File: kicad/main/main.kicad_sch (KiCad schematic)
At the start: 20 parts, among them U1 DS1813-5+, U2 L7805, U3 Z80CPU, U4 74HC00, U5 AS6C4008-55PCN, U6 74HC273, U7 27C512, X1 4 MHz

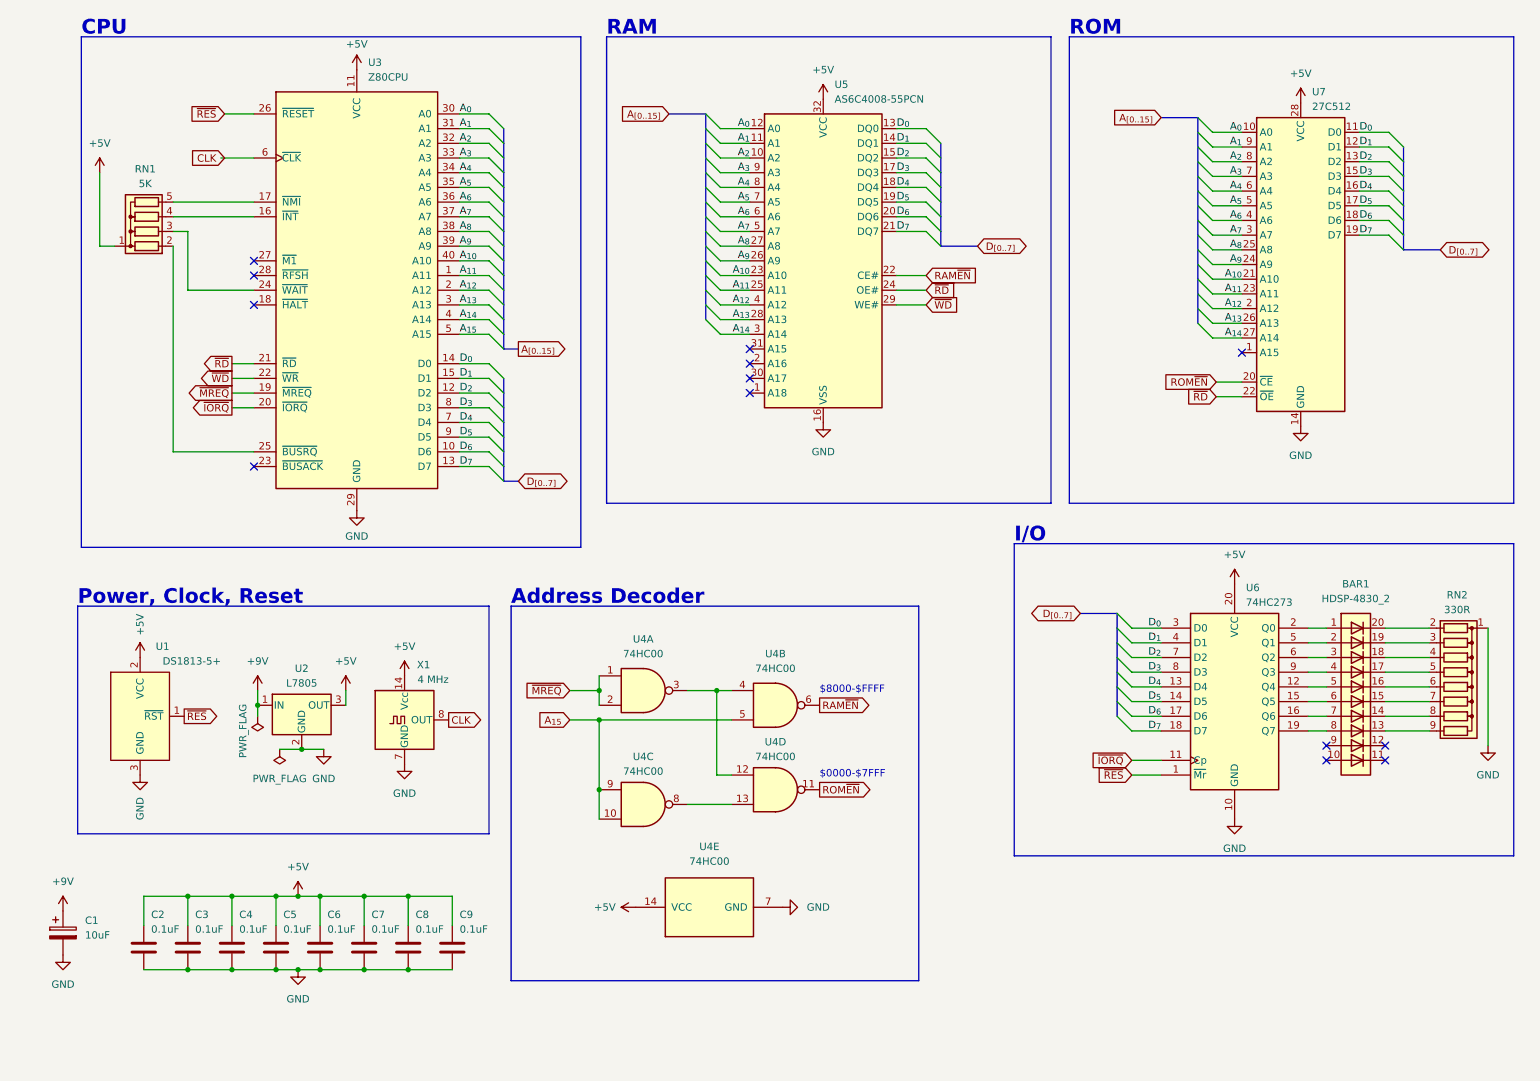
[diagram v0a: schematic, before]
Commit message: Smaller KiCad symbols, reset button
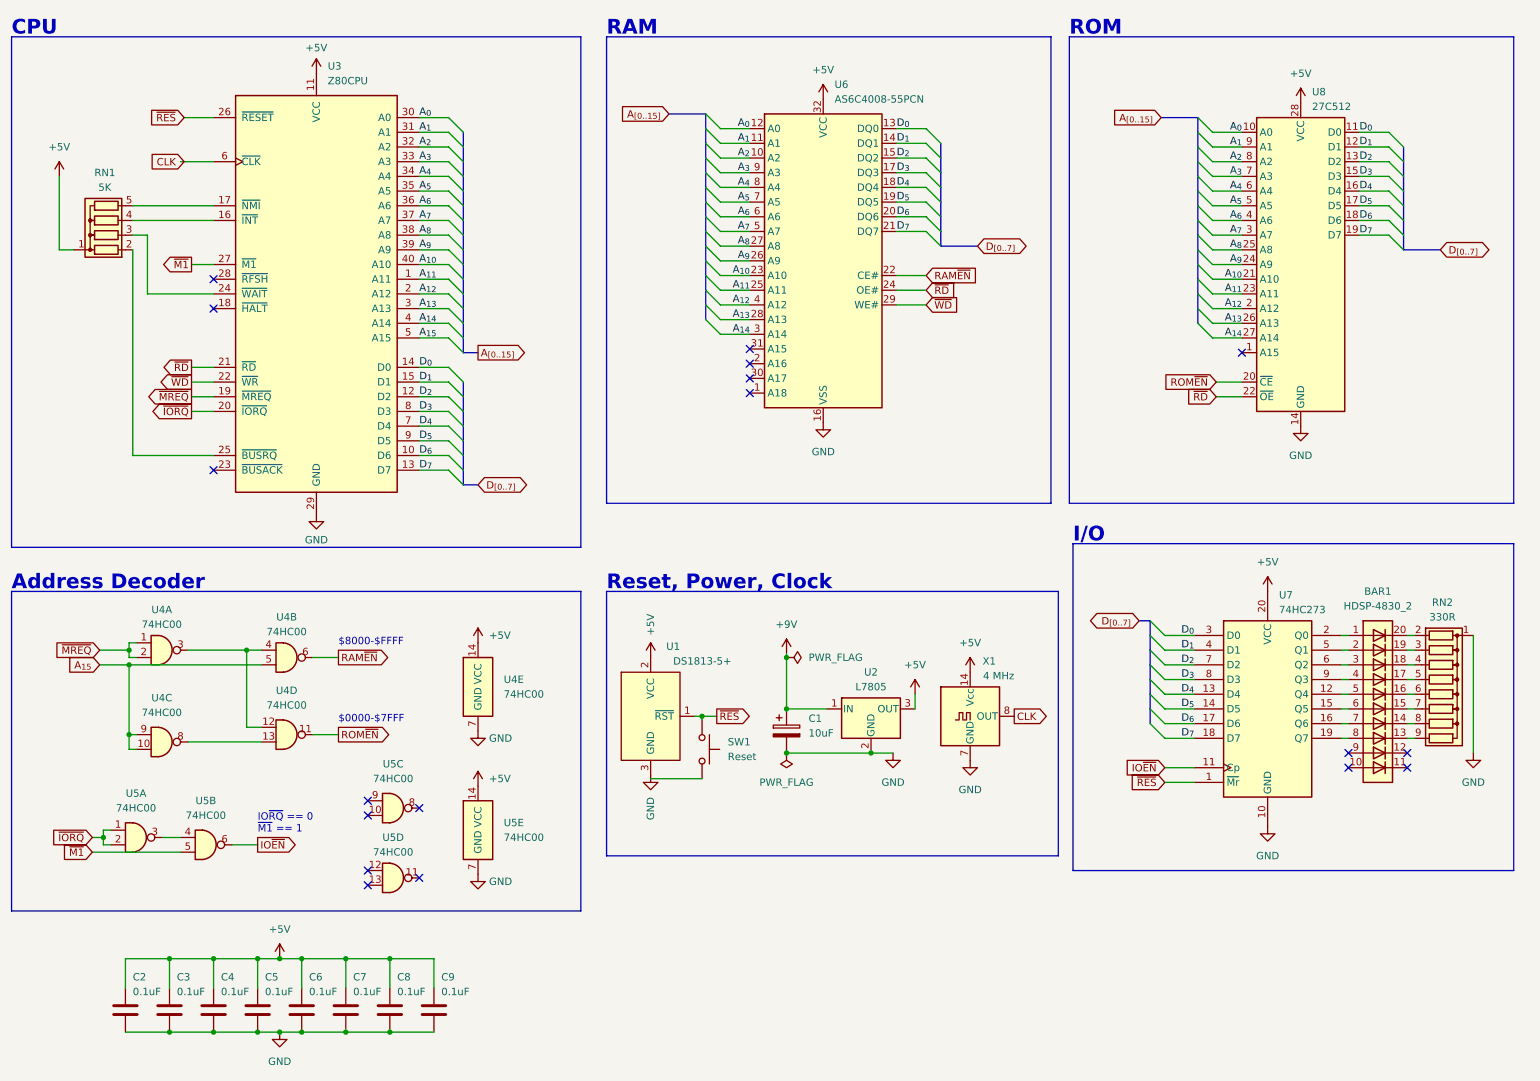
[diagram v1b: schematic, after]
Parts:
- added SW1: Reset, Button_Switch_THT:SW_PUSH_6mm, symbol Switch:SW_Push
- added U5: 74HC00, Package_DIP:DIP-14_W7.62mm_Socket, symbol 74hc00_small:74HC00
- U4: symbol 74xx:74HC00 -> 74hc00_small:74HC00
- renumbered U5 to U6, U6 to U7, U7 to U8
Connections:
- net +5V: now also U5.14 (VCC)
- net GND: now also U5.7 (GND)
- net ~{IORQ}: now also U5.1, U5.2; no longer U7.11 (Cp)
- net ~{RES}: now also SW1.2
- net ~{M1}: now reaches U3.27 (~{M1})
- net ~{M1}: now also U5.5
- new net: U5.3, U5.4
- new net IO~{EN}: U5.6, U7.11 (Cp)
- no-connect marks 13 -> 18
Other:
- note added: "IO~{RQ} == 0 ~{M1} == 1"
- note added: "Reset, Power, Clock"
- note removed: "Power, Clock, Reset"
- moved on the sheet: BAR1, C2, C3, C4, C5, C6, C7, C8, C9, RN1, RN2, U1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

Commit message: Basic PCB
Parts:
- added J1: Barrel_Jack_MountingPin, Connector_BarrelJack:BarrelJack_GCT_DCJ200-10-A_Horizontal, symbol Connector:Barrel_Jack_MountingPin
- added RN3: 5K, Resistor_THT:R_Array_SIP9, symbol Device:R_Network08
- added SW2: SW_DIP_x08, Button_Switch_THT:SW_DIP_SPSTx08_Slide_9.78x22.5mm_W7.62mm_P2.54mm, symbol Switch:SW_DIP_x08
- added U1: 74HC00, Package_DIP:DIP-14_W7.62mm_Socket, symbol 74hc00_small:74HC00
- added U10: 74HC244, Package_DIP:DIP-20_W7.62mm_Socket, symbol 74xx:74HC244
- U9: renamed from U8; footprint Package_DIP:DIP-28_W15.24mm -> my:ZIF28
- renumbered C2 to C1, C3 to C2, C4 to C3, C5 to C4, C6 to C5, C7 to C6, C8 to C7, C9 to C8, C1 to C9, U5 to U2, U4 to U3, U3 to U4, U1 to U5, U2 to U7, U7 to U8
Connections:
- net +5V: now also RN3.1 (common), U1.14 (VCC), U10.20 (VCC)
- net A_{0}: now also U1.10, U1.12, U1.9
- net D_{0}: now also U10.18 (1Y0)
- net D_{1}: now also U10.16 (1Y1)
- net D_{2}: now also U10.14 (1Y2)
- net D_{3}: now also U10.12 (1Y3)
- net D_{4}: now also U10.3 (2Y0)
- net D_{5}: now also U10.5 (2Y1)
- net D_{6}: now also U10.7 (2Y2)
- net D_{7}: now also U10.9 (2Y3)
- net GND: now also SW1.2, J1.2, SW2.1, SW2.2, SW2.3, SW2.4, SW2.5, SW2.6, SW2.7, SW2.8, U1.7 (GND), U10.10 (GND)
- net IO~{EN}: now also U1.1, U1.2; no longer U8.11 (Cp)
- net ~{RES}: now also SW1.1; no longer SW1.2
- net +9V: no longer names the net of C9.1, U7.1 (IN)
- net +9V: now also J1.1
- new net: RN3.8 (R7), SW2.10, U10.13 (2A2)
- new net: RN3.7 (R6), SW2.11, U10.15 (2A1)
- new net: RN3.6 (R5), SW2.12, U10.17 (2A0)
- new net: RN3.5 (R4), SW2.13, U10.8 (1A3)
- new net: RN3.4 (R3), SW2.14, U10.6 (1A2)
- new net: RN3.3 (R2), SW2.15, U10.4 (1A1)
- new net: RN3.2 (R1), SW2.16, U10.2 (1A0)
- new net: RN3.9 (R8), SW2.9, U10.11 (2A3)
- new net: U1.13, U1.3, U1.4
- new net: U1.5, U1.8
- new net IN~{EN}: U1.6, U10.1 (1OE), U10.19 (2OE)
- new net OUT~{EN}: U1.11, U8.11 (Cp)
- no-connect marks 18 -> 19
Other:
- note added: "Port 0"
- note added: "Port 1"
- note added: "Power, Reset, Clock"
- note removed: "Reset, Power, Clock"
- moved on the sheet: BAR1, C1, C2, C3, C4, C5, C6, C7, C8, C9, RN2, SW1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

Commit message: First PCB
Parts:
- removed U1, U2, U3: 74HC00, Package_DIP:DIP-14_W7.62mm_Socket, symbol 74hc00_small:74HC00
- added U1: GAL16V8, Package_DIP:DIP-20_W7.62mm_Socket, symbol Logic_Programmable:GAL16V8
- C1, C3, C4, C6, C7, C8: footprint Capacitor_THT:C_Disc_D3.0mm_W1.6mm_P2.50mm -> my:C_Disc_Long
- C2: footprint Capacitor_THT:C_Disc_D3.0mm_W1.6mm_P2.50mm -> my:C_Disc_Medium
- renumbered U4 to U2, U5 to U3, U6 to U4, U7 to U5, U8 to U6, U9 to U7, U10 to U8
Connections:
- net +5V: now also U1.20 (VCC)
- net A_{0}: now also U1.3 (I3)
- net A_{15}: now also U1.4 (I4)
- net GND: now also U1.10 (GND), U1.11 (I10/~{OE})
- net IN~{EN}: now also U1.15 (IO5)
- net OUT~{EN}: now also U1.16 (IO4)
- net RAM~{EN}: now also U1.13 (IO7)
- net ROM~{EN}: now also U1.12 (IO8)
- net ~{IORQ}: now also U1.5 (I5)
- net ~{M1}: now also U1.6 (I6)
- net ~{MREQ}: now also U1.2 (I2)
- no-connect marks 19 -> 21
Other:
- note added: "IO~{RQ} == 0, ~{M1} == 1"
- note removed: "IO~{RQ} == 0 ~{M1} == 1"
- note removed: "Port 0"
- note removed: "Port 1"
- moved on the sheet: C1, C2, C3, C4, C5, C6, C7, C8

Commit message: PCB update + Gerber
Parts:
- added H1, H2, H3, H4: MountingHole, MountingHole:MountingHole_3.2mm_M3_Pad, symbol Mechanical:MountingHole
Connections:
- net +5V: now also U1.1 (I1/CLK)
- net GND: now also U1.7 (I7), U1.8 (I8), U1.9 (I9), U4.1 (A18), U4.2 (A16), U4.30 (A17), U4.31 (A15), U7.1 (A15)
- no-connect marks 21 -> 12
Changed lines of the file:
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@@
   (junction (at 302.26 171.45) (diameter 0) (color 0 0 0 0)
   )
+  (junction (at 153.67 76.835) (diameter 0) (color 0 0 0 0)
+  )
   (junction (at 167.005 149.225) (diameter 0) (color 0 0 0 0)
   )
@@
   (junction (at 302.26 168.91) (diameter 0) (color 0 0 0 0)
   )
+  (junction (at 153.67 79.375) (diameter 0) (color 0 0 0 0)
+  )
   (junction (at 333.375 173.99) (diameter 0) (color 0 0 0 0)
   )
@@
   (junction (at 167.005 156.845) (diameter 0) (color 0 0 0 0)
   )
+  (junction (at 57.785 146.685) (diameter 0) (color 0 0 0 0)
+  )
   (junction (at 320.675 161.29) (diameter 0) (color 0 0 0 0)
   )
@@
   (junction (at 57.785 182.245) (diameter 0) (color 0 0 0 0)
   )
+  (junction (at 45.085 174.625) (diameter 0) (color 0 0 0 0)
+  )
   (junction (at 302.26 173.99) (diameter 0) (color 0 0 0 0)
   )
@@
   (junction (at 83.82 231.775) (diameter 0) (color 0 0 0 0)
   )
+  (junction (at 166.37 84.455) (diameter 0) (color 0 0 0 0)
+  )
   (junction (at 83.82 219.075) (diameter 0) (color 0 0 0 0)
   )
+  (junction (at 257.175 85.09) (diameter 0) (color 0 0 0 0)
+  )
   (junction (at 302.26 163.83) (diameter 0) (color 0 0 0 0)
   )
@@
   (junction (at 45.72 231.775) (diameter 0) (color 0 0 0 0)
   )
+  (junction (at 153.67 74.295) (diameter 0) (color 0 0 0 0)
+  )
   (junction (at 64.77 231.775) (diameter 0) (color 0 0 0 0)
   )
@@
   (junction (at 150.495 180.975) (diameter 0) (color 0 0 0 0)
   )
+  (junction (at 45.085 172.085) (diameter 0) (color 0 0 0 0)
+  )
+  (junction (at 45.085 169.545) (diameter 0) (color 0 0 0 0)
+  )
   (no_connect (at 73.66 164.465))
-  (no_connect (at 45.085 167.005))
-  (no_connect (at 247.015 72.39))
   (no_connect (at 274.32 177.165))
   (no_connect (at 51.435 64.77))
-  (no_connect (at 45.085 151.765))
-  (no_connect (at 153.67 71.755))
   (no_connect (at 51.435 92.71))
   (no_connect (at 274.32 179.705))
   (no_connect (at 148.59 159.385))
   (no_connect (at 264.16 177.165))
-  (no_connect (at 45.085 172.085))
-  (no_connect (at 153.67 76.835))
   (no_connect (at 70.485 154.305))
-  (no_connect (at 153.67 74.295))
-  (no_connect (at 45.085 169.545))
-  (no_connect (at 153.67 79.375))
   (no_connect (at 264.16 179.705))
   (no_connect (at 70.485 156.845))
@@
     (stroke (width 0) (type default))
   )
+  (wire (pts (xy 153.67 79.375) (xy 153.67 84.455))
+    (stroke (width 0) (type default))
+  )
   (wire (pts (xy 247.015 54.61) (xy 241.935 54.61))
     (stroke (width 0) (type default))
@@
     (stroke (width 0) (type default))
   )
+  (wire (pts (xy 245.11 72.39) (xy 245.11 85.09))
+    (stroke (width 0) (type default))
+  )
   (wire (pts (xy 86.995 46.99) (xy 92.075 46.99))
     (stroke (width 0) (type default))
@@
     (stroke (width 0) (type default))
   )
+  (wire (pts (xy 45.085 167.005) (xy 45.085 169.545))
+    (stroke (width 0) (type default))
+  )
   (bus (pts (xy 186.69 36.195) (xy 186.69 38.735))
     (stroke (width 0) (type default))
@@
     (stroke (width 0) (type default))
   )
+  (wire (pts (xy 247.015 72.39) (xy 245.11 72.39))
+    (stroke (width 0) (type default))
+  )
   (bus (pts (xy 94.615 59.69) (xy 94.615 62.23))
     (stroke (width 0) (type default))
@@
     (stroke (width 0) (type default))
   )
+  (wire (pts (xy 45.085 151.765) (xy 43.815 151.765))
+    (stroke (width 0) (type default))
+  )
   (wire (pts (xy 267.335 41.91) (xy 272.415 41.91))
     (stroke (width 0) (type default))
@@
     (stroke (width 0) (type default))
   )
+  (wire (pts (xy 153.67 71.755) (xy 153.67 74.295))
+    (stroke (width 0) (type default))
+  )
   (bus (pts (xy 146.05 31.115) (xy 139.7 31.115))
     (stroke (width 0) (type default))
@@
     (stroke (width 0) (type default))
   )
+  (wire (pts (xy 43.815 151.765) (xy 43.815 146.685))
+    (stroke (width 0) (type default))
+  )
   (wire (pts (xy 73.66 164.465) (xy 70.485 164.465))
     (stroke (width 0) (type default))
@@
     (stroke (width 0) (type default))
   )
+  (wire (pts (xy 43.815 146.685) (xy 57.785 146.685))
+    (stroke (width 0) (type default))
+  )
   (wire (pts (xy 51.435 77.47) (xy 47.625 77.47))
     (stroke (width 0) (type default))
@@
     (stroke (width 0) (type default))
   )
+  (wire (pts (xy 153.67 84.455) (xy 166.37 84.455))
+    (stroke (width 0) (type default))
+  )
   (wire (pts (xy 153.67 48.895) (xy 148.59 48.895))
     (stroke (width 0) (type default))
   )
+  (wire (pts (xy 45.085 169.545) (xy 45.085 172.085))
+    (stroke (width 0) (type default))
+  )
   (wire (pts (xy 86.995 82.55) (xy 92.075 82.55))
     (stroke (width 0) (type default))
@@
     (stroke (width 0) (type default))
   )
+  (wire (pts (xy 45.085 172.085) (xy 45.085 174.625))
+    (stroke (width 0) (type default))
+  )
   (bus (pts (xy 274.955 46.99) (xy 274.955 49.53))
     (stroke (width 0) (type default))
@@
     (stroke (width 0) (type default))
   )
+  (wire (pts (xy 153.67 76.835) (xy 153.67 79.375))
+    (stroke (width 0) (type default))
+  )
   (wire (pts (xy 150.495 180.975) (xy 149.225 180.975))
     (stroke (width 0) (type default))
   )
+  (wire (pts (xy 153.67 74.295) (xy 153.67 76.835))
+    (stroke (width 0) (type default))
+  )
   (bus (pts (xy 274.955 41.91) (xy 274.955 44.45))
     (stroke (width 0) (type default))
@@
     (stroke (width 0) (type default))
   )
+  (wire (pts (xy 245.11 85.09) (xy 257.175 85.09))
+    (stroke (width 0) (type default))
+  )
   (wire (pts (xy 86.995 80.01) (xy 92.075 80.01))
     (stroke (width 0) (type default))
@@
     )
   )
+  (symbol (lib_id "Mechanical:MountingHole") (at 121.285 222.25 0) (unit 1)
+    (in_bom yes) (on_board yes) (dnp no) (fields_autoplaced)
+    (property "Reference" "H2" (at 124.46 220.98 0)
+      (effects (font (size 1.27 1.27)) (justify left))
+    )
+    (property "Value" "MountingHole" (at 124.46 223.52 0)
+      (effects (font (size 1.27 1.27)) (justify left))
+    )
+    (property "Footprint" "MountingHole:MountingHole_3.2mm_M3_Pad" (at 121.285 222.25 0)
+      (effects (font (size 1.27 1.27)) hide)
+    )
+    (property "Datasheet" "~" (at 121.285 222.25 0)
+      (effects (font (size 1.27 1.27)) hide)
+    )
+    (instances
+      (project "main"
+        (path "/234daa3c-bbc3-4e0e-9846-fc4a6309b941"
+          (reference "H2") (unit 1)
+        )
+      )
+    )
+  )
   (symbol (lib_id "power:GND") (at 257.175 85.09 0) (unit 1)
     (in_bom yes) (on_board yes) (dnp no) (fields_autoplaced)
@@
     )
   )
+  (symbol (lib_id "Mechanical:MountingHole") (at 121.285 234.95 0) (unit 1)
+    (in_bom yes) (on_board yes) (dnp no) (fields_autoplaced)
+    (property "Reference" "H4" (at 124.46 233.68 0)
+      (effects (font (size 1.27 1.27)) (justify left))
+    )
+    (property "Value" "MountingHole" (at 124.46 236.22 0)
+      (effects (font (size 1.27 1.27)) (justify left))
+    )
+    (property "Footprint" "MountingHole:MountingHole_3.2mm_M3_Pad" (at 121.285 234.95 0)
+      (effects (font (size 1.27 1.27)) hide)
+    )
+    (property "Datasheet" "~" (at 121.285 234.95 0)
+      (effects (font (size 1.27 1.27)) hide)
+    )
+    (instances
+      (project "main"
+        (path "/234daa3c-bbc3-4e0e-9846-fc4a6309b941"
+          (reference "H4") (unit 1)
+        )
+      )
+    )
+  )
   (symbol (lib_id "Connector:Barrel_Jack_MountingPin") (at 148.59 151.765 0) (unit 1)
     (in_bom yes) (on_board yes) (dnp no) (fields_autoplaced)
@@
     )
   )
+  (symbol (lib_id "Mechanical:MountingHole") (at 121.285 228.6 0) (unit 1)
+    (in_bom yes) (on_board yes) (dnp no) (fields_autoplaced)
+    (property "Reference" "H3" (at 124.46 227.33 0)
+      (effects (font (size 1.27 1.27)) (justify left))
+    )
+    (property "Value" "MountingHole" (at 124.46 229.87 0)
+      (effects (font (size 1.27 1.27)) (justify left))
+    )
+    (property "Footprint" "MountingHole:MountingHole_3.2mm_M3_Pad" (at 121.285 228.6 0)
+      (effects (font (size 1.27 1.27)) hide)
+    )
+    (property "Datasheet" "~" (at 121.285 228.6 0)
+      (effects (font (size 1.27 1.27)) hide)
+    )
+    (instances
+      (project "main"
+        (path "/234daa3c-bbc3-4e0e-9846-fc4a6309b941"
+          (reference "H3") (unit 1)
+        )
+      )
+    )
+  )
   (symbol (lib_id "power:+5V") (at 257.175 29.21 0) (unit 1)
     (in_bom yes) (on_board yes) (dnp no) (fields_autoplaced)
@@
         )
       )
+    )
+  )
+  (symbol (lib_id "Mechanical:MountingHole") (at 121.285 215.9 0) (unit 1)
+    (in_bom yes) (on_board yes) (dnp no) (fields_autoplaced)
+    (property "Reference" "H1" (at 124.46 214.63 0)
+      (effects (font (size 1.27 1.27)) (justify left))
+    )
+    (property "Value" "MountingHole" (at 124.46 217.17 0)
+      (effects (font (size 1.27 1.27)) (justify left))
+    )
+    (property "Footprint" "MountingHole:MountingHole_3.2mm_M3_Pad" (at 121.285 215.9 0)
+      (effects (font (size 1.27 1.27)) hide)
+    )
+    (property "Datasheet" "~" (at 121.285 215.9 0)
+      (effects (font (size 1.27 1.27)) hide)
+    )
+    (instances
+      (project "main"
+        (path "/234daa3c-bbc3-4e0e-9846-fc4a6309b941"
+          (reference "H1") (unit 1)
+        )
+      )
